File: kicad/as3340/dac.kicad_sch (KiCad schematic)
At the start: 26 parts

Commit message: kicad library fix...again
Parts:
- C16, C25, C39: value (none) -> 0.1u; footprint (none) -> Capacitor_SMD:C_0603_1608Metric
- C24, C5: value (none) -> 4.7u; footprint (none) -> Capacitor_SMD:C_0805_2012Metric
- R47: value (none) -> 4k7; footprint (none) -> Resistor_SMD:R_1206_3216Metric
- R48: value (none) -> 100k; footprint (none) -> Resistor_SMD:R_0603_1608Metric
- R49: renamed from R?; value (none) -> 10k .1%; footprint (none) -> Resistor_SMD:R_0603_1608Metric
- R50: renamed from R?; value (none) -> 30k .1%; footprint (none) -> Resistor_SMD:R_0603_1608Metric
- R51: renamed from R?; value (none) -> 100k; footprint (none) -> Resistor_SMD:R_0603_1608Metric
- R52, R53: renamed from R?; value (none) -> 8k2; footprint (none) -> Resistor_SMD:R_0603_1608Metric
- R54, R55: renamed from R?; value (none) -> 33k; footprint (none) -> Resistor_SMD:R_0603_1608Metric
- R61: renamed from R?; value (none) -> 10k; footprint (none) -> Resistor_SMD:R_0603_1608Metric
- R64: renamed from R?; value (none) -> 15k; footprint (none) -> Resistor_SMD:R_0603_1608Metric
- R67: renamed from R?; value (none) -> 51k; footprint (none) -> Resistor_SMD:R_0603_1608Metric
- R68: value (none) -> 10k; footprint (none) -> Resistor_SMD:R_0603_1608Metric
- R69: value (none) -> 30k; footprint (none) -> Resistor_SMD:R_0603_1608Metric
- TP3: value (none) -> TestPoint; footprint (none) -> TestPoint:TestPoint_Pad_2.0x2.0mm
- U12: renamed from U?; value (none) -> TL074; footprint (none) -> Package_SO:SOIC-14_3.9x8.7mm_P1.27mm
- U13: value (none) -> LM4040AIM3-2.5; footprint (none) -> Package_TO_SOT_THT:TO-92_Inline_Wide
- U14: value (none) -> TLV5610IDW; footprint (none) -> Package_SO:SOIC-20W_7.5x12.8mm_P1.27mm
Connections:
- net FREQ_CV_DAC: now also U12.8; no longer U12.14
- net FREQ_CV_FROM_DAC: now also U12.10 (+); no longer U12.12 (+)
- net GND: now also U12.3 (+); no longer U12.5 (+)
- net LINEAR_FM_DAC: now also U12.7; no longer U12.14
- net LINEAR_FM_FROM_DAC: now also U12.5 (+); no longer U12.12 (+)
- net PWM_DAC: now also U12.1; no longer U12.7
- net at R49.1, R50.2: now also U12.9 (-); no longer U12.13 (-)
- net at R48.2, R51.2, R67.1: now also U12.6 (-); no longer U12.13 (-)
- net at R61.1, R64.2: now also U12.2 (-); no longer U12.6 (-)

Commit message: remove rescue library
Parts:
- U14: symbol as3340-rescue:TLV5610IDW-Audio -> as3340:TLV5610IDW-Audio
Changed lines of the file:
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@@
     (pin "2")
   )
-  (symbol (lib_id "as3340-rescue:TLV5610IDW-Audio") (at 110.49 58.42 0) (unit 1)
+  (symbol (lib_id "as3340:TLV5610IDW-Audio") (at 110.49 58.42 0) (unit 1)
     (in_bom yes) (on_board yes)
     (property "Reference" "U14" (id 0) (at 107.95 73.66 0))

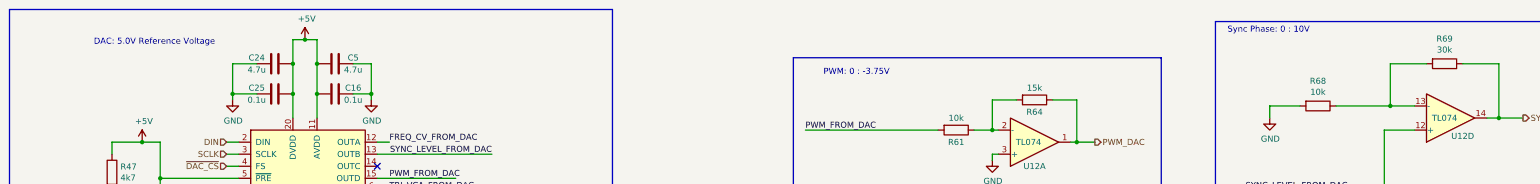
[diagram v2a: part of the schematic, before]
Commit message: schematic changes, still need values
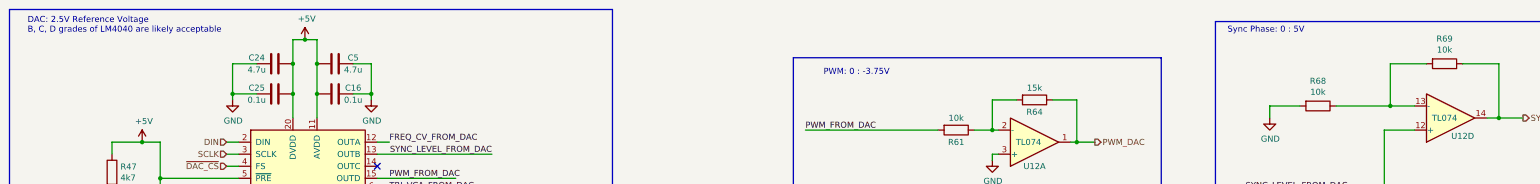
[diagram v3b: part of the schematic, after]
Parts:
- R69: value 30k -> 10k; LCSC Part C22984 -> C25804
- U13: footprint Package_TO_SOT_THT:TO-92_Inline_Wide -> Package_TO_SOT_SMD:SOT-23; LCSC Part (none) -> C131939; jlcpcb C140239 -> (none)
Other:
- note added: "DAC: 2.5V Reference Voltage B, C, D grades of LM4040 are likely acceptable"
- note added: "Sync Phase: 0 : 5V"
- note removed: "DAC: 5.0V Reference Voltage"
- note removed: "Sync Phase: 0 : 10V"
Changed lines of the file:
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@@
     (effects (font (size 1.27 1.27)) (justify left bottom))
   )
-  (text "Sync Phase: 0 : 10V" (at 302.26 38.1 0)
+  (text "Sync Phase: 0 : 5V" (at 302.26 38.1 0)
     (effects (font (size 1.27 1.27)) (justify left bottom))
   )
@@
     (effects (font (size 1.27 1.27)) (justify left bottom))
   )
-  (text "DAC: 5.0V Reference Voltage" (at 63.5 40.64 0)
+  (text "DAC: 2.5V Reference Voltage\nB, C, D grades of LM4040 are likely acceptable"
+    (at 49.53 38.1 0)
     (effects (font (size 1.27 1.27)) (justify left bottom))
   )
@@
       (effects (font (size 1.27 1.27)) (justify right))
     )
-    (property "Footprint" "Package_TO_SOT_THT:TO-92_Inline_Wide" (id 2) (at 72.39 78.74 0)
+    (property "Footprint" "Package_TO_SOT_SMD:SOT-23" (id 2) (at 72.39 78.74 0)
       (effects (font (size 1.27 1.27) italic) hide)
     )
@@
       (effects (font (size 1.27 1.27) italic) hide)
     )
-    (property "jlcpcb" "C140239" (id 4) (at 67.31 78.74 90)
-      (effects (font (size 1.27 1.27)) hide)
-    )
-    (property "LCSC Part" "" (id 5) (at 67.31 78.74 0)
+    (property "LCSC Part" "C131939" (id 5) (at 67.31 78.74 0)
       (effects (font (size 1.27 1.27)) hide)
     )
@@
     (in_bom yes) (on_board yes)
     (property "Reference" "R69" (id 0) (at 347.98 39.1922 90))
-    (property "Value" "30k" (id 1) (at 347.98 41.5036 90))
+    (property "Value" "10k" (id 1) (at 347.98 41.5036 90))
     (property "Footprint" "Resistor_SMD:R_0603_1608Metric" (id 2) (at 347.98 42.672 90)
       (effects (font (size 1.27 1.27)) hide)
@@
       (effects (font (size 1.27 1.27)) hide)
     )
-    (property "LCSC Part" "C22984" (id 4) (at 347.98 44.45 0)
-      (effects (font (size 1.27 1.27)) hide)
-    )
+    (property "LCSC Part" "C25804" (id 4) (at 347.98 44.45 0)
+      (effects (font (size 1.27 1.27)) hide)
+    )

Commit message: fixes for BOM
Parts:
- C16, C25, C39: LCSC C14663 -> (none)
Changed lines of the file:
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@@
-      (effects (font (size 1.27 1.27)) hide)
-    )
-    (property "LCSC" "" (id 4) (at 114.3 44.45 90)
       (effects (font (size 1.27 1.27)) hide)
     )
@@
       (effects (font (size 1.27 1.27)) hide)
     )
-    (property "LCSC" "C14663" (id 4) (at 114.3 50.8 90)
-      (effects (font (size 1.27 1.27)) hide)
-    )
     (property "LCSC Part" "C14663" (id 5) (at 114.3 50.8 0)
       (effects (font (size 1.27 1.27)) hide)
@@
       (effects (font (size 1.27 1.27)) hide)
     )
-    (property "LCSC" "" (id 4) (at 101.6 44.45 90)
-      (effects (font (size 1.27 1.27)) hide)
-    )
     (property "LCSC Part" "C1779" (id 5) (at 101.6 44.45 0)
       (effects (font (size 1.27 1.27)) hide)
@@
     )
     (property "Datasheet" "~" (id 3) (at 101.6 50.8 0)
-      (effects (font (size 1.27 1.27)) hide)
-    )
-    (property "LCSC" "C14663" (id 4) (at 101.6 50.8 90)
       (effects (font (size 1.27 1.27)) hide)
     )
@@
       (effects (font (size 1.27 1.27)) hide)
     )
-    (property "LCSC" "C14663" (id 4) (at 55.88 78.74 90)
-      (effects (font (size 1.27 1.27)) hide)
-    )

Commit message: update title block and add schematic pdf
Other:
- title: Zoxnoxious 3340 DAC -> Zoxnoxious 3340 Oscillator
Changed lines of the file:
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@@
   (paper "B")
   (title_block
-    (title "Zoxnoxious 3340 DAC")
-    (rev "0.3")
+    (title "Zoxnoxious 3340 Oscillator")
+    (rev "0.4")
     (company "Zoxnoxious Engineering")
   )

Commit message: updates to 0.4 as3340 and 0.3 backplane
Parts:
- removed C16: 0.1u, Capacitor_SMD:C_0603_1608Metric, symbol Device:C
- removed C5: 4.7u, Capacitor_SMD:C_0805_2012Metric, symbol Device:C
- removed U14: TLV5610IDW, Package_SO:SOIC-20W_7.5x12.8mm_P1.27mm, symbol as3340:TLV5610IDW-Audio
- added U14: AD5328, Package_SO:TSSOP-16_4.4x5mm_P0.65mm, symbol as3340:AD5328
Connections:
- net +5V: now also C24.1, C25.1, U14.3 (VDD); no longer C24.2, C25.2
- net DAC_TEST: now also U14.12 (VOUT_G)
- net DIN: now also U14.15 (DIN)
- net FREQ_CV_FROM_DAC: now also U14.4 (VOUT_A)
- net GND: now also C24.2, C25.2, U14.1 (~{LDAC}), U14.14 (GND); no longer C24.1, C25.1
- net LINEAR_FM_FROM_DAC: now also U14.13 (VOUT_H)
- net OSC_EXT_VCA_FROM_DAC: now also U14.11 (VOUT_F)
- net PWM_FROM_DAC: now also U14.7 (VOUT_D)
- net SCLK: now also U14.16 (SCLK)
- net SYNC_LEVEL_FROM_DAC: now also U14.5 (VOUT_B)
- net TRI_VCA_FROM_DAC: now also U14.10 (VOUT_E)
- net VREF_2.5V: now also U14.8 (VREF_ABCD), U14.9 (VREF_EFGH)
- net ~{DAC_CS}: now also U14.2 (~{SYNC})
- no-connect marks 2 -> 1
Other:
- moved on the sheet: C24, C25, C39, R47, TP3, U13

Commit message: add 3340 v0.4 gerbers
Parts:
- U12: LCSC Part C12594 -> C6963
- U14: LCSC Part (none) -> C29162
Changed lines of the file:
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@@
       (effects (font (size 1.27 1.27)) hide)
     )
-    (property "LCSC Part" "C12594" (id 4) (at 261.62 60.96 0)
+    (property "LCSC Part" "C6963" (id 4) (at 261.62 60.96 0)
       (effects (font (size 1.27 1.27)) hide)
     )
@@
       (effects (font (size 1.27 1.27)) hide)
     )
-    (property "LCSC Part" "C12594" (id 4) (at 349.25 55.88 0)
+    (property "LCSC Part" "C6963" (id 4) (at 349.25 55.88 0)
       (effects (font (size 1.27 1.27)) hide)
     )
@@
       (effects (font (size 1.27 1.27)) hide)
     )
-    (property "LCSC Part" "C12594" (id 4) (at 123.19 146.05 0)
+    (property "LCSC Part" "C6963" (id 4) (at 123.19 146.05 0)
       (effects (font (size 1.27 1.27)) hide)
     )
@@
       (effects (font (size 1.27 1.27)) hide)
     )
-    (property "LCSC Part" "C12594" (id 4) (at 133.35 185.42 0)
+    (property "LCSC Part" "C6963" (id 4) (at 133.35 185.42 0)
       (effects (font (size 1.27 1.27)) hide)
     )
@@
       (effects (font (size 1.27 1.27)) hide)
     )
+    (property "LCSC Part" "C29162" (id 4) (at 100.33 71.12 0)
+      (effects (font (size 1.27 1.27)) hide)
+    )

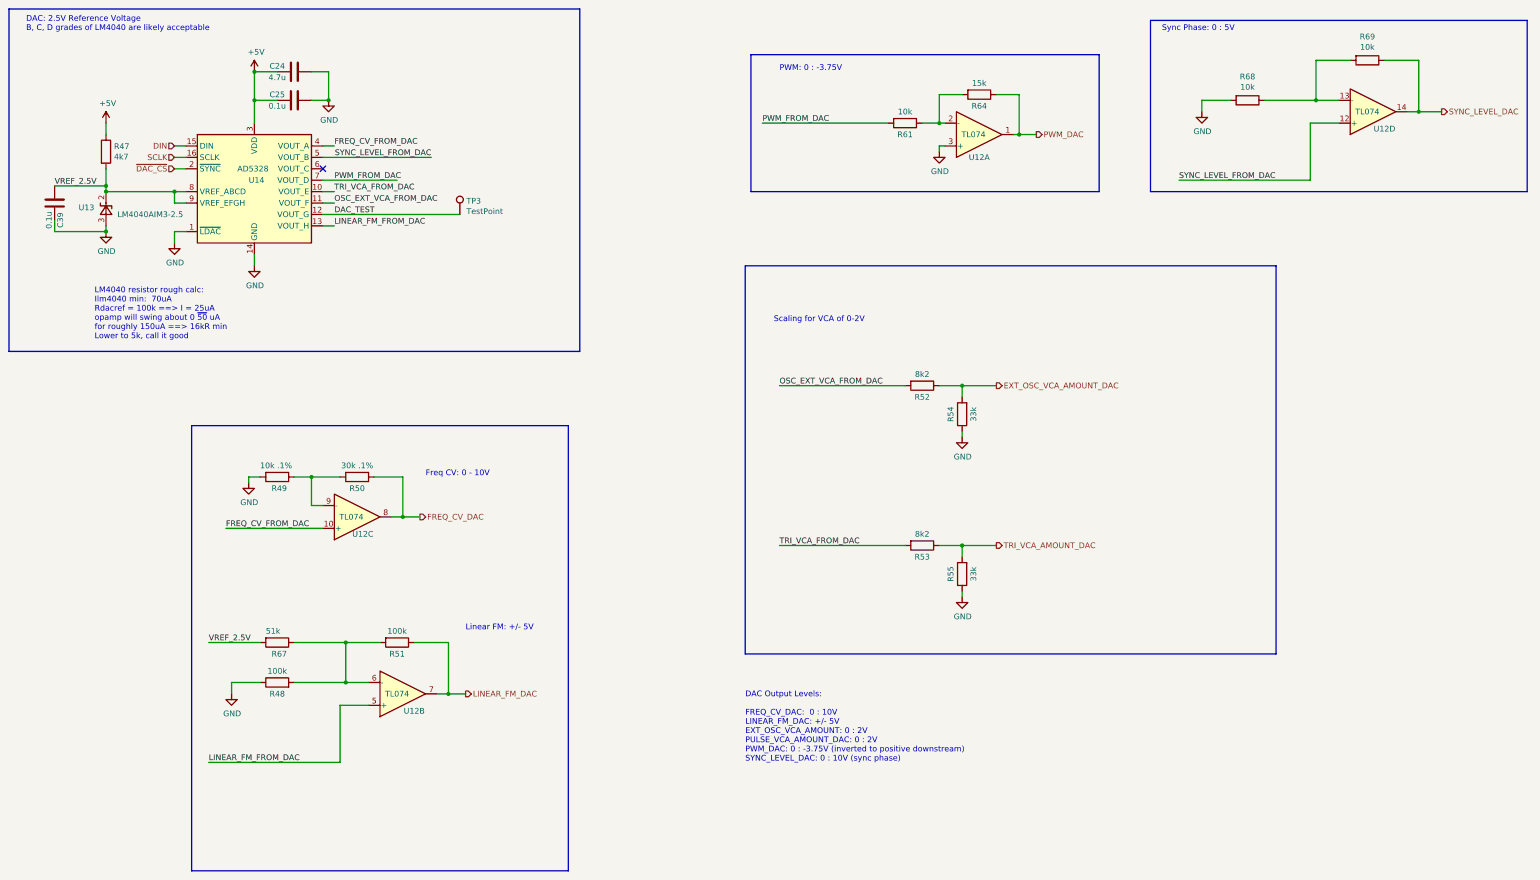
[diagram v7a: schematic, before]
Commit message: starting updates for v0.5
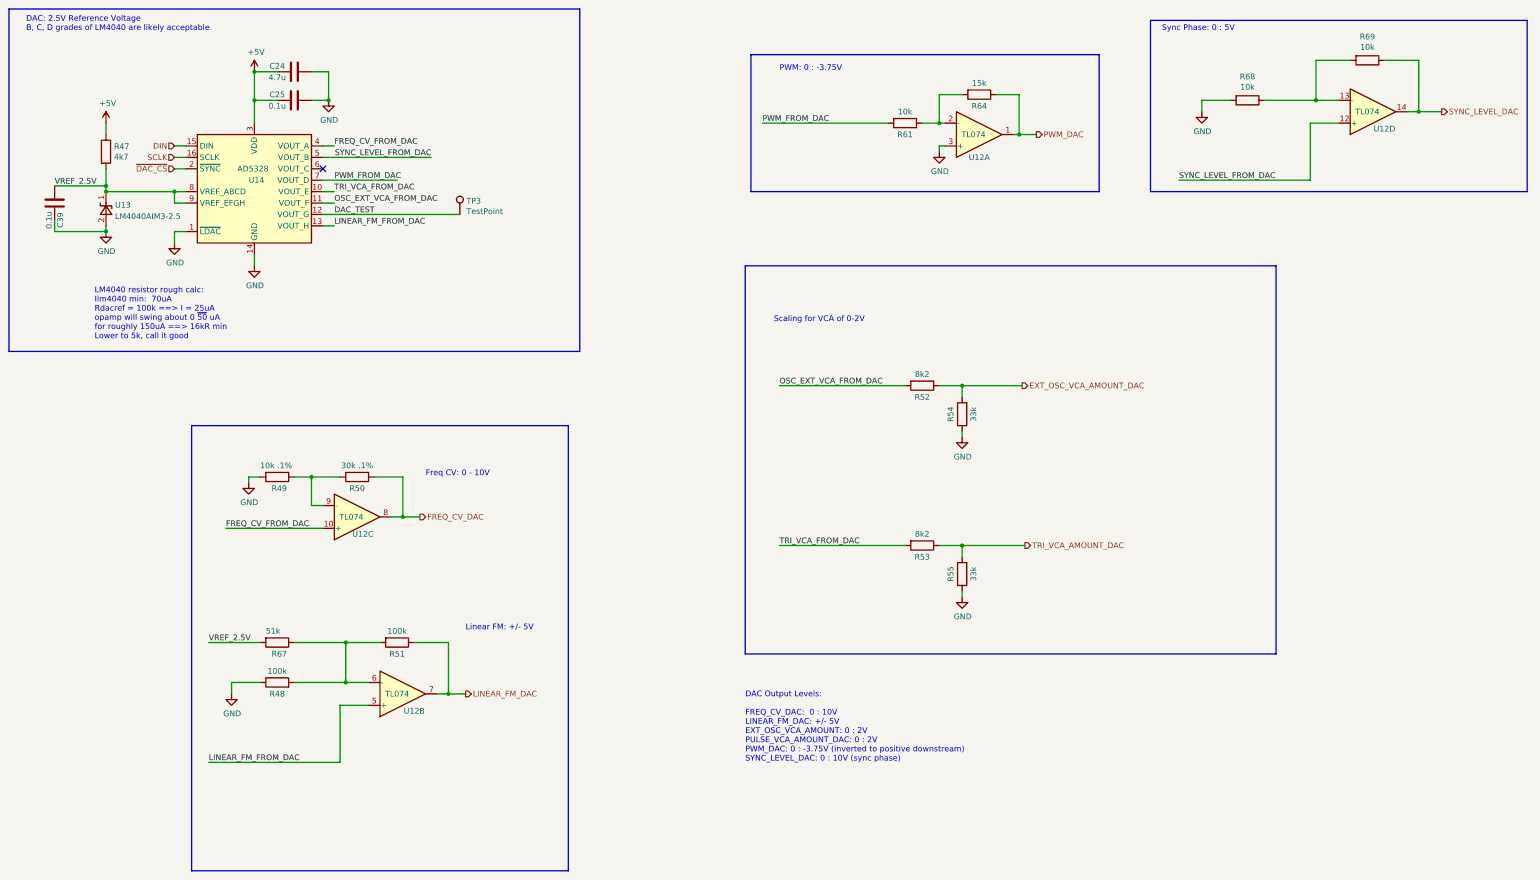
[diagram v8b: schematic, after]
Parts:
- removed U13: LM4040AIM3-2.5, Package_TO_SOT_SMD:SOT-23, symbol Reference_Voltage:LM4040LP-4.1
- added U13: LM4040AIM3-2.5, Package_TO_SOT_SMD:SOT-23, symbol Reference_Voltage:LM4040DBZ-2.5
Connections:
- net GND: now also U13.2 (A)
- net VREF_2.5V: now also U13.1 (K)
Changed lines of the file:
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@@
   (junction (at 257.81 152.4) (diameter 0) (color 0 0 0 0)
   )
+  (junction (at 67.31 72.39) (diameter 0) (color 0 0 0 0)
+  )
+  (junction (at 82.55 73.66) (diameter 0) (color 0 0 0 0)
+  )
   (junction (at 100.33 53.34) (diameter 0) (color 0 0 0 0)
   )
@@
   (junction (at 120.65 173.99) (diameter 0) (color 0 0 0 0)
   )
+  (junction (at 67.31 82.55) (diameter 0) (color 0 0 0 0)
+  )
   (junction (at 257.81 116.84) (diameter 0) (color 0 0 0 0)
   )
@@
   (junction (at 252.73 58.42) (diameter 0) (color 0 0 0 0)
   )
-  (junction (at 67.31 72.39) (diameter 0) (color 0 0 0 0)
-  )
   (junction (at 120.65 182.88) (diameter 0) (color 0 0 0 0)
   )
-  (junction (at 67.31 82.55) (diameter 0) (color 0 0 0 0)
-  )
   (junction (at 100.33 46.99) (diameter 0) (color 0 0 0 0)
   )
   (junction (at 143.51 185.42) (diameter 0) (color 0 0 0 0)
   )
+  (junction (at 359.41 55.88) (diameter 0) (color 0 0 0 0)
+  )
   (junction (at 67.31 73.66) (diameter 0) (color 0 0 0 0)
-  )
-  (junction (at 359.41 55.88) (diameter 0) (color 0 0 0 0)
-  )
-  (junction (at 82.55 73.66) (diameter 0) (color 0 0 0 0)
   )
   (no_connect (at 115.57 68.58))
@@
     (stroke (width 0) (type default) (color 0 0 0 0))
   )
-  (wire (pts (xy 67.31 73.66) (xy 82.55 73.66))
-    (stroke (width 0) (type default) (color 0 0 0 0))
-  )
   (wire (pts (xy 115.57 78.74) (xy 146.05 78.74))
     (stroke (width 0) (type default) (color 0 0 0 0))
@@
     (stroke (width 0) (type default) (color 0 0 0 0))
   )
-  (wire (pts (xy 257.81 116.84) (xy 265.43 116.84))
+  (wire (pts (xy 257.81 116.84) (xy 271.145 116.84))
     (stroke (width 0) (type default) (color 0 0 0 0))
   )
@@
     (stroke (width 0) (type default) (color 0 0 0 0))
   )
+  (wire (pts (xy 82.55 73.66) (xy 67.31 73.66))
+    (stroke (width 0) (type default) (color 0 0 0 0))
+  )
   (polyline (pts (xy 170.18 125.73) (xy 170.18 224.79))
     (stroke (width 0) (type default) (color 0 0 0 0))
@@
     (stroke (width 0) (type default) (color 0 0 0 0))
   )
-  (wire (pts (xy 257.81 152.4) (xy 265.43 152.4))
+  (wire (pts (xy 257.81 152.4) (xy 271.78 152.4))
     (stroke (width 0) (type default) (color 0 0 0 0))
   )
@@
     (stroke (width 0) (type default) (color 0 0 0 0))
   )
+  (wire (pts (xy 67.31 81.28) (xy 67.31 82.55))
+    (stroke (width 0) (type default) (color 0 0 0 0))
+  )
   (wire (pts (xy 311.15 53.34) (xy 317.5 53.34))
     (stroke (width 0) (type default) (color 0 0 0 0))
@@
     (stroke (width 0) (type default) (color 0 0 0 0))
   )
+  (wire (pts (xy 67.31 73.66) (xy 67.31 72.39))
+    (stroke (width 0) (type default) (color 0 0 0 0))
+  )
   (polyline (pts (xy 45.72 33.02) (xy 172.72 33.02))
     (stroke (width 0) (type default) (color 0 0 0 0))
@@
     (stroke (width 0) (type default) (color 0 0 0 0))
   )
-  (wire (pts (xy 67.31 81.28) (xy 67.31 82.55))
-    (stroke (width 0) (type default) (color 0 0 0 0))
-  )
   (wire (pts (xy 359.41 44.45) (xy 359.41 55.88))
     (stroke (width 0) (type default) (color 0 0 0 0))
@@
   )
   (wire (pts (xy 143.51 185.42) (xy 147.32 185.42))
-    (stroke (width 0) (type default) (color 0 0 0 0))
-  )
-  (wire (pts (xy 67.31 73.66) (xy 67.31 72.39))
     (stroke (width 0) (type default) (color 0 0 0 0))
   )
@@
     (effects (font (size 1.27 1.27)) (justify left bottom))
   )
-  (hierarchical_label "EXT_OSC_VCA_AMOUNT_DAC" (shape output) (at 265.43 116.84 0)
+  (hierarchical_label "EXT_OSC_VCA_AMOUNT_DAC" (shape output) (at 271.145 116.84 0)
     (effects (font (size 1.27 1.27)) (justify left))
   )
@@
     (effects (font (size 1.27 1.27)) (justify left))
   )
-  (hierarchical_label "TRI_VCA_AMOUNT_DAC" (shape output) (at 265.43 152.4 0)
+  (hierarchical_label "TRI_VCA_AMOUNT_DAC" (shape output) (at 271.78 152.4 0)
     (effects (font (size 1.27 1.27)) (justify left))
   )
@@
     (pin "1")
   )
-  (symbol (lib_id "Reference_Voltage:LM4040LP-4.1") (at 67.31 77.47 90) (unit 1)
-    (in_bom yes) (on_board yes)
-    (property "Reference" "U13" (id 0) (at 61.214 77.216 90)
-      (effects (font (size 1.27 1.27)) (justify right))
-    )
-    (property "Value" "LM4040AIM3-2.5" (id 1) (at 69.85 78.74 90)
-      (effects (font (size 1.27 1.27)) (justify right))
-    )
-    (property "Footprint" "Package_TO_SOT_SMD:SOT-23" (id 2) (at 72.39 77.47 0)
-      (effects (font (size 1.27 1.27) italic) hide)
-    )
-    (property "Datasheet" "http://www.ti.com/lit/ds/symlink/lm4040-n.pdf" (id 3) (at 67.31 77.47 0)
-      (effects (font (size 1.27 1.27) italic) hide)
-    )
-    (property "LCSC Part" "C131939" (id 5) (at 67.31 77.47 0)
-      (effects (font (size 1.27 1.27)) hide)
-    )
-    (property "Digikey" "LM4040BIZ-2.5/NOPB-ND" (id 6) (at 67.31 77.47 0)
-      (effects (font (size 1.27 1.27)) hide)
-    )
-    (pin "2")
-    (pin "3")
-  )
   (symbol (lib_id "Device:R") (at 67.31 64.77 0) (unit 1)
     (in_bom yes) (on_board yes)
@@
     (pin "1")
   )
+  (symbol (lib_id "Reference_Voltage:LM4040DBZ-2.5") (at 67.31 77.47 90) (unit 1)
+    (in_bom yes) (on_board yes) (fields_autoplaced)
+    (property "Reference" "U13" (id 0) (at 69.3166 76.6353 90)
+      (effects (font (size 1.27 1.27)) (justify right))
+    )
+    (property "Value" "LM4040AIM3-2.5" (id 1) (at 69.3166 79.1722 90)
+      (effects (font (size 1.27 1.27)) (justify right))
+    )
+    (property "Footprint" "Package_TO_SOT_SMD:SOT-23" (id 2) (at 72.39 77.47 0)
+      (effects (font (size 1.27 1.27) italic) hide)
+    )
+    (property "Datasheet" "http://www.ti.com/lit/ds/symlink/lm4040-n.pdf" (id 3) (at 67.31 77.47 0)
+      (effects (font (size 1.27 1.27) italic) hide)
+    )
+    (property "LCSC Part" "C131939" (id 4) (at 67.31 77.47 90)
+      (effects (font (size 1.27 1.27)) hide)
+    )
+    (pin "1")
+    (pin "2")
+  )
   (symbol (lib_id "as3340:AD5328") (at 100.33 71.12 0) (unit 1)
